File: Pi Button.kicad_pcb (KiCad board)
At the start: 2 copper layers, 5 parts, among them J1 Conn_02x20_Odd_Even, SW1 SW_Push, SW2 SW_Push

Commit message: part placement
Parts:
- J1: moved to B.Cu
- R1, R2: footprint Resistor_SMD:R_0805_2012Metric -> Resistor_THT:R_Axial_DIN0204_L3.6mm_D1.6mm_P2.54mm_Vertical
- moved SW1 144.1 mm to (128.5, 81.5)
- moved SW2 130.8 mm to (128.5, 62.5)
- moved R1 123.5 mm to (114.5, 82.0)
- moved R2 113.3 mm to (114.5, 62.0)
- moved J1 106.2 mm to (96.0, 50.8), turned to 180 degrees
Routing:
- net Net-(J1-Pin_18): track 0.00 -> 36.1 mm
- net Net-(J1-Pin_16): track 0.00 -> 30.6 mm
- net Net-(R2-Pad2): track 0.00 -> 11.7 mm
- net Net-(R1-Pad2): track 0.00 -> 11.7 mm
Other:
- board outline added: 50 x 55 mm

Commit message: v1
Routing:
- added copper zone on B.Cu, net GND
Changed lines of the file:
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@@
+	)
+	(segment
+		(start 114.46 62)
+		(end 114.389 62.071)
+		(width 0.2)
+		(layer "B.Cu")
+		(net 39)
 	)
 	(segment
@@
 		(net 42)
 	)
+	(zone
+		(net 39)
+		(net_name "GND")
+		(layer "B.Cu")
+		(hatch edge 0.5)
+		(connect_pads
+			(clearance 0.5)
+		)
+		(min_thickness 0.25)
+		(filled_areas_thickness no)
+		(fill yes
+			(thermal_gap 0.5)
+			(thermal_bridge_width 0.5)
+		)
+		(polygon
+			(pts
+				(xy 91 46) (xy 91 103) (xy 143 103) (xy 143 46)
+			)
+		)
+	)
 	(embedded_fonts no)

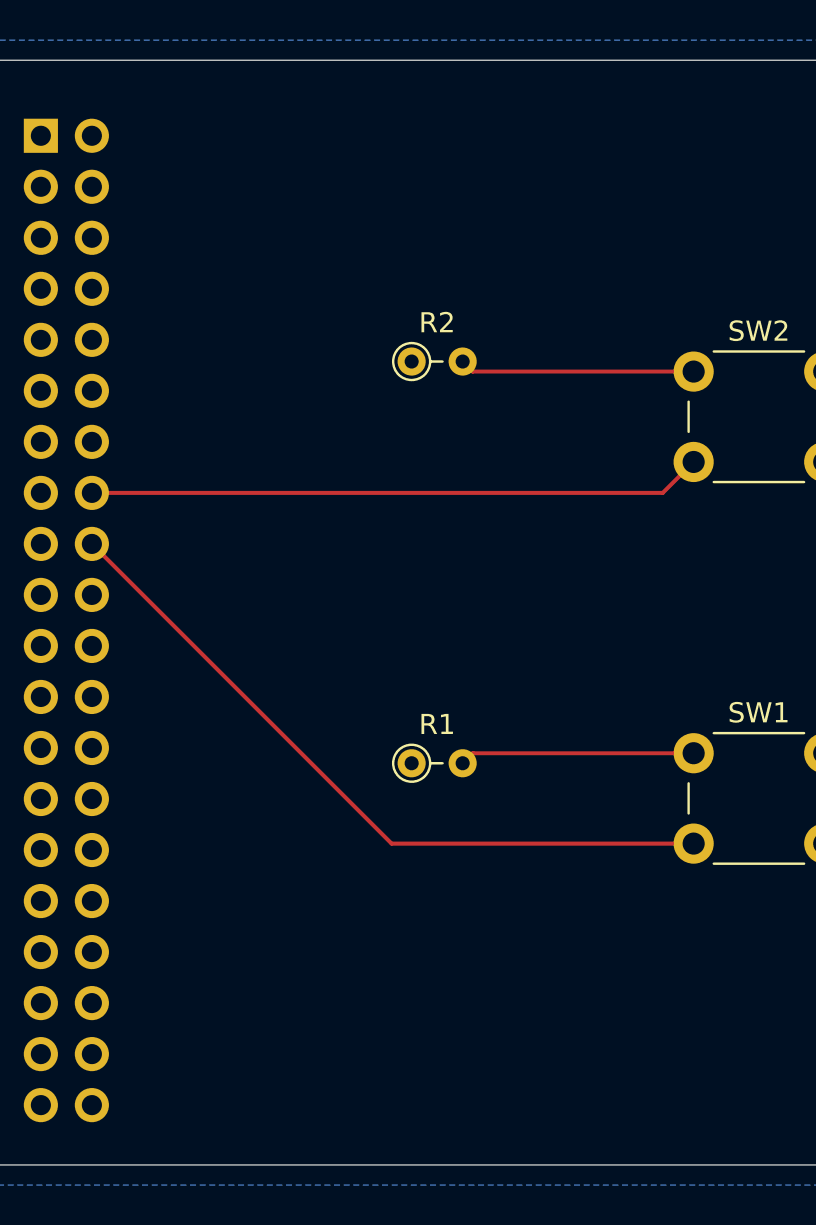
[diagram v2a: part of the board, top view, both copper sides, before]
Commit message: changed resistors and silk screen
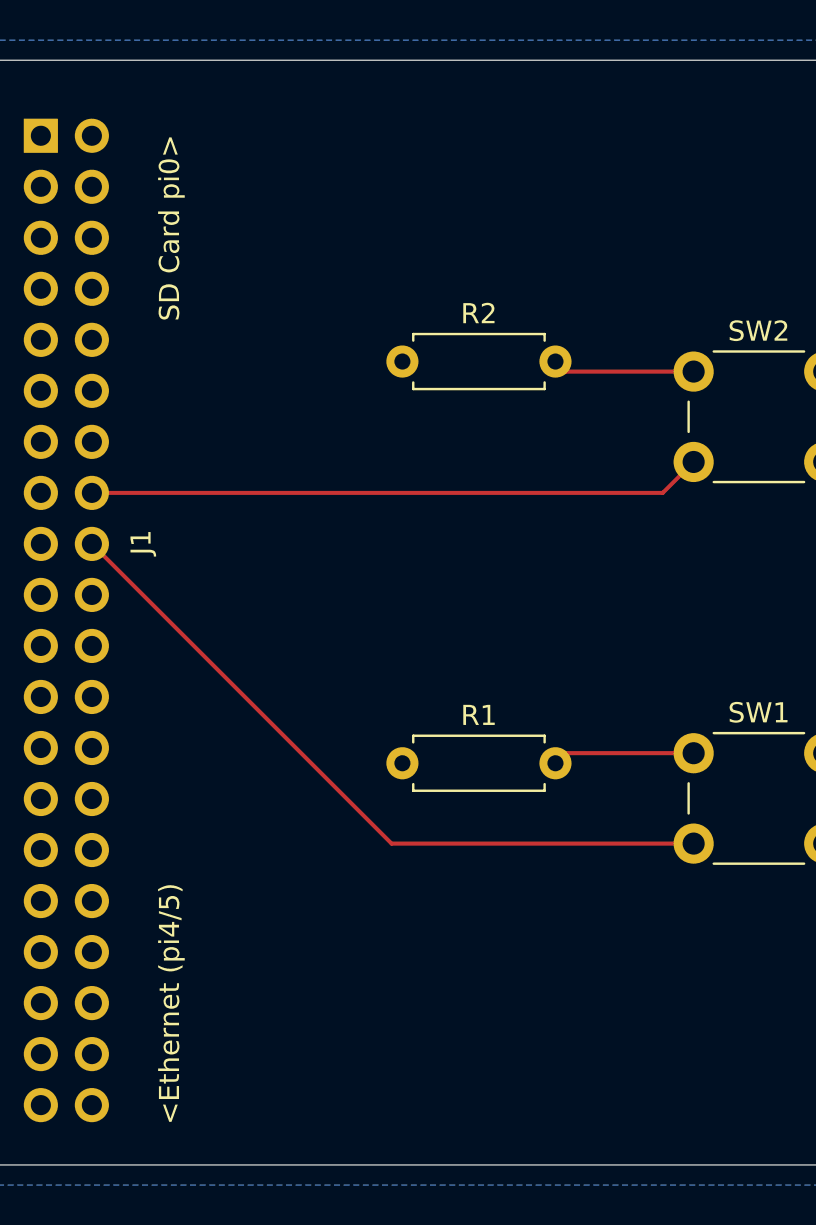
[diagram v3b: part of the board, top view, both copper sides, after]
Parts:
- R1, R2: footprint Resistor_THT:R_Axial_DIN0204_L3.6mm_D1.6mm_P2.54mm_Vertical -> Resistor_THT:R_Axial_DIN0207_L6.3mm_D2.5mm_P7.62mm_Horizontal
- moved R1 0.46 mm to (114.0, 82.0)
- moved R2 0.46 mm to (114.0, 62.0)
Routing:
- net Net-(R1-Pad2): track 11.7 -> 7.09 mm
- net Net-(R2-Pad2): track 11.7 -> 7.29 mm
- net GND: track 0.20 -> 1.41 mm
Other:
- board text added: "<Ethernet (pi4/5)"
- board text added: "SD Card pi0>"
